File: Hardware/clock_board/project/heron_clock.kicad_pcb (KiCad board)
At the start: 4 copper layers, 84 x 56 mm, 110 parts, among them J1 5V_IN, J10 PPS_B200_2, J2 PPS_IN, J3 REF_B210_1, J4 REF_B210_2, J5 REF_B200_1, J6 REF_B200_2, J7 PPS_B210_1, J8 PPS_B210_2, J9 PPS_B200_1, U1 TPS7A2033DBVR, U2 TPS7A2033DBVR, U3 SiT5155AI-FK-33E0-10.000000, U4 LMK1C1104PWR, U5 SN74LVC1G17DBVR, U6 SN74LVC125APWR

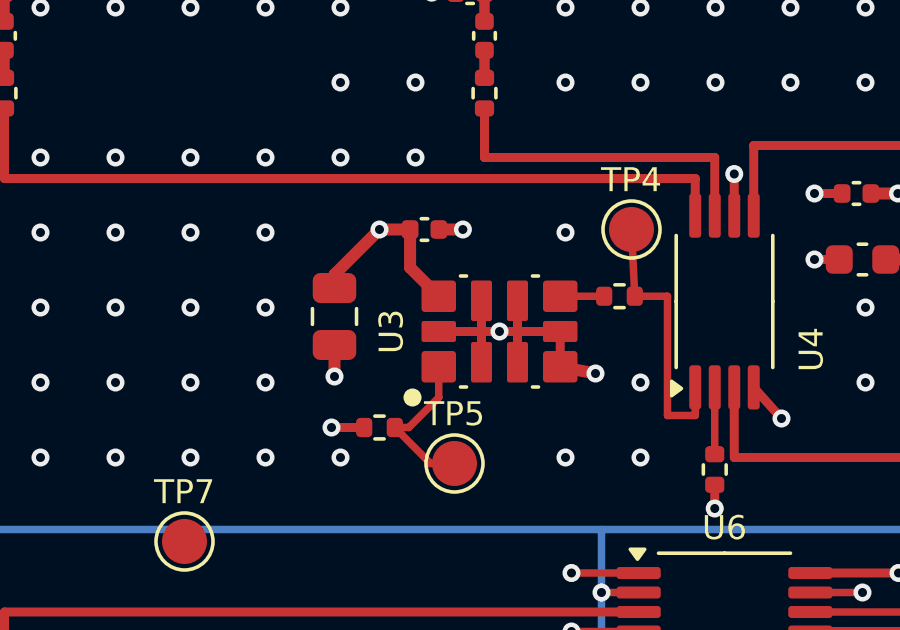
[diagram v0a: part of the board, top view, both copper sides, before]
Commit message: Move C8 next to SiT5155 VDD pin and add GND vias at U3 (D-026)
Put C8 (100 nF) 1.7 mm from U3 pin 9, per SiT5155 datasheet p.35. Add three GND vias at U3 pins 2, 3 and 7. Regenerate the board, fab outputs and project file with KiCad 7. DRC: 0 errors. Record D-026: the TCXO stays fixed-frequency, with no I2C. Update CLAUDE.md sync line and repository map.
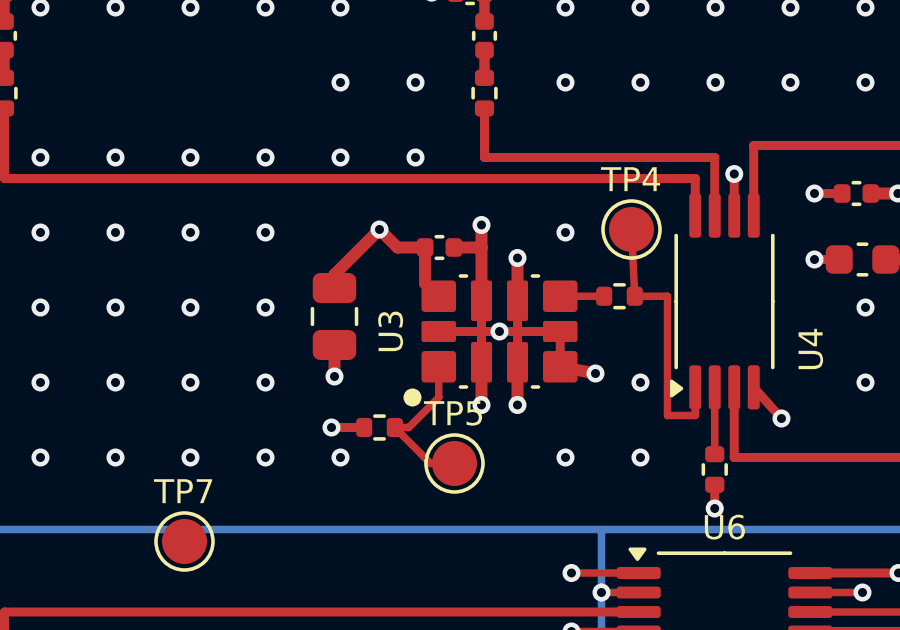
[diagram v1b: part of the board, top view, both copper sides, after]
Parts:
- moved C8 0.78 mm to (134.5, 129.2)
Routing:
- net GND: track 67.1 -> 74.0 mm, vias 447 -> 450
